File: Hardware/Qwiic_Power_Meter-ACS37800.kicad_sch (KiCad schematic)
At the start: 31 parts, among them J1 Conn_01x01, J10 Conn_01x01, J11 Conn_01x01, J12 I2C, J3 Qwiic_RA, J4 Conn_01x01, J5 Conn_01x01, J6 Conn_01x01, J7 Qwiic_RA, J8 Conn_01x01, J9 Conn_01x01, U1 ACS37800

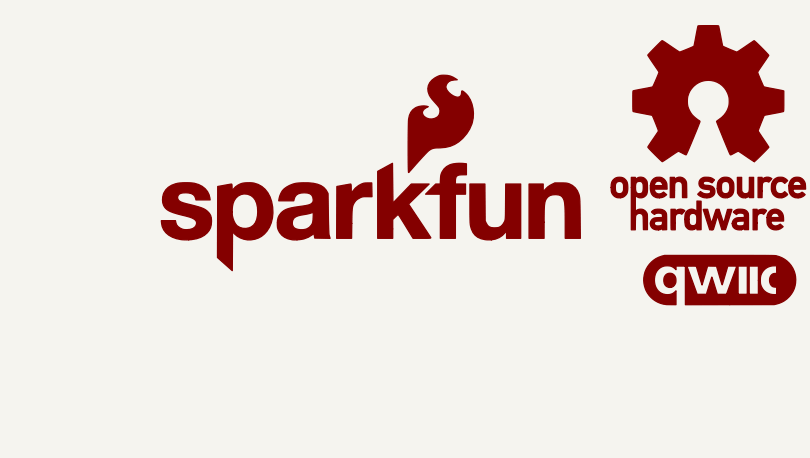
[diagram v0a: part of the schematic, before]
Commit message: Adds fiducials and standoffs, changes the silk on the underside
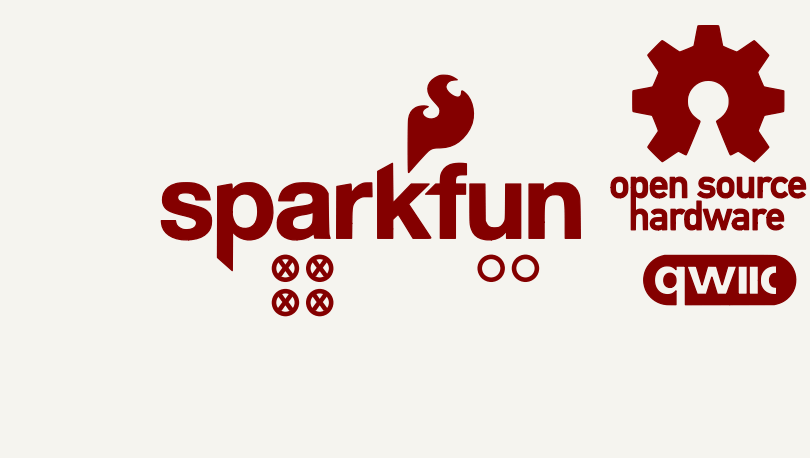
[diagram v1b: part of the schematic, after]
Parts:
- added FID1, FID2, FID3, FID4: Fiducial_0.5mm, SparkFun-Aesthetic:Fiducial_0.5mm_Mask1mm, symbol SparkFun-Aesthetic:Fiducial_0.5mm
- added ST1, ST2: Standoff, SparkFun-Hardware:Standoff, symbol SparkFun-Hardware:Standoff

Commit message: Updates 1x01 labels in the schematic, fixes some jumper labels
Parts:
- J4: value Conn_01x01 -> HI
- J5: value Conn_01x01 -> LO
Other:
- note added: "Make sure to keep this jumper closed."
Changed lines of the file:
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@@
 		)
 	)
+	(text "Make sure to keep this jumper closed. "
+		(exclude_from_sim no)
+		(at 130.81 62.865 0)
+		(effects
+			(font
+				(size 1.27 1.27)
+			)
+		)
+	)
 	(text "Default 7-bit unshifted I^{2}C Addres: 0x60"
 		(exclude_from_sim no)
@@
 		)
 	)
+	(polyline
+		(pts
+			(xy 108.585 62.865) (xy 111.76 62.865)
+		)
+		(stroke
+			(width 0)
+			(type dot)
+		)
+	)
 	(wire
 		(pts
@@
 		)
 	)
+	(polyline
+		(pts
+			(xy 108.585 60.325) (xy 108.585 62.865)
+		)
+		(stroke
+			(width 0)
+			(type dot)
+		)
+	)
 	(wire
 		(pts
@@
 			)
 		)
-		(property "Value" "Conn_01x01"
+		(property "Value" "HI"
 			(at 73.66 50.7999 0)
 			(effects
@@
 				)
 				(justify left)
+				(hide yes)
 			)
 		)
@@
 		(dnp no)
 		(property "Reference" "IP+1"
-			(at 78.994 42.672 0)
+			(at 78.74 43.18 0)
 			(effects
 				(font
@@
 					(size 1.27 1.27)
 				)
+				(hide yes)
 			)
 		)
@@
 		(on_board yes)
 		(dnp no)
-		(fields_autoplaced yes)
 		(property "Reference" "J5"
 			(at 73.406 53.34 0)
@@
 			)
 		)
-		(property "Value" "Conn_01x01"
-			(at 73.66 53.3399 0)
+		(property "Value" "LO"
+			(at 72.39 53.34 0)
 			(effects
 				(font
 					(size 1.27 1.27)
 				)
-				(justify left)
 			)
 		)
